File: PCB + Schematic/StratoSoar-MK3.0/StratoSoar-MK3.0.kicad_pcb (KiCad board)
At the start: 4 copper layers, 36.6 x 55.2 mm, 81 parts, among them J1 Signal, J2 Power, J3 Button, J4 USB-C, J5 J Link, J6 Antenna, J7 Battery, J8 Rudder, J9 Rudder, Q1 BSS138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

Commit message: Silkscreen!
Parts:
- removed J6: Antenna, Connector_PinHeader_2.54mm:PinHeader_1x01_P2.54mm_Vertical
- removed JP2: ERR_LED_EN, Jumper:SolderJumper-2_P1.3mm_Open_RoundedPad1.0x1.5mm
- added AE2: Antenna, Connector_PinHeader_2.54mm:PinHeader_1x01_P2.54mm_Vertical, B.Cu at (159.8, 98.8)
- added G***: LOGO, LOGO, B.Cu at (176.2, 96.2)
- added G***: LOGO, LOGO, B.Cu at (132.1, 108.1)
- JP1: value LED_EN -> ALWAYS_ON
- moved JP1 21.6 mm to (183.5, 104.5), turned to 180 degrees
- moved J4 0.73 mm to (190.8, 94.1)
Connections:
- JP1 pad 1: Net-(JP3-A) -> VCC
- JP1 pad 2: LED -> +BATT
- R10 pad 2: Net-(JP3-A) -> LED
- R14 pad 2: Net-(JP2-A) -> ERR
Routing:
- net VCC: track 55.2 -> 61.7 mm, vias 1 -> 2
- net +BATT: track 40.2 -> 43.7 mm
- net D-: track 23.8 -> 25.1 mm
- net Net-(JP3-A): track 1.13 -> 0.00 mm, vias 1 -> 0
- net Net-(JP2-A): track 1.13 -> 0.00 mm, vias 1 -> 0
- net ERR: track 9.07 -> 8.19 mm, vias 1 -> 0
- net D+: track 22.3 -> 23.1 mm
- net GND: track 102.3 -> 103.0 mm
- net Net-(J4-CC2): track 1.66 -> 2.39 mm
- net Net-(J4-CC1): track 1.70 -> 2.42 mm
- net LED: track 4.22 -> 3.66 mm, vias 1 -> 0
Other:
- board text added: "BTN"
- board text added: "Designed by Charlie Nicholson, July 2024"
- board text added: "EEPROM"
- board text added: "JLCJLCJLCJLC"
- board text added: "JP1 = Solder to enable always on"
- board text added: "Left servo-"
- board text added: "Licensed under CERN-OHL-S-2.0"
- board text added: "OFF"
- board text added: "ON"
- board text added: "RF"
- board text added: "Right servo-"
- board text added: "USB"
- board text added: "https://github.com/ crnicholson/StratoSoar-MK3"

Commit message: RF, silkscreen
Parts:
- added G***: LOGO, LOGO, B.Cu at (176.8, 83.7)
- added G***: LOGO, LOGO, B.Cu at (176.9, 88.5)
- moved G*** 11.5 mm to (169.3, 105.4)
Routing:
- net CS: track 34.1 -> 44.8 mm
- net R_FET: track 29.1 -> 39.2 mm
- net MOSI: track 44.4 -> 54.5 mm
- net MISO: track 37.1 -> 46.6 mm
- net SCK: track 39.4 -> 47.5 mm
- net RIGHT: track 39.4 -> 46.2 mm
- net LEFT: track 43.7 -> 50.1 mm
- net L_FET: track 59.7 -> 64.4 mm
- net Net-(AE2-Pin_1): track 21.6 -> 23.3 mm
- net BATT: track 32.2 -> 33.9 mm
- net SWCLK: track 11.8 -> 13.4 mm
- net SCL: track 57.9 -> 56.2 mm
- net SDA: track 60.2 -> 59.1 mm
- net GPS_EN: track 42.5 -> 43.3 mm
- net GND: track 103.0 -> 102.9 mm, vias 78 -> 84
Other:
- board text added: "Made possible by:"
- board text added: "NEWbs"
- board text added: "New England Weather Balloon Society"

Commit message: Finished PCB
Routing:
- net SCK: track 47.5 -> 57.6 mm
- net MISO: track 46.6 -> 51.2 mm, vias 2 -> 1
- net MOSI: track 54.5 -> 57.7 mm
- net L_FET: track 64.4 -> 63.4 mm
- net CS: track 44.8 -> 43.9 mm
- net R_FET: track 39.2 -> 39.9 mm
- net GND: vias 84 -> 106
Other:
- board text added: "POWER"

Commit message: Actually finished board for real?
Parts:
- added H3: MountingHole, MountingHole:MountingHole_2.2mm_M2, F.Cu at (2.48, 2.48)
- C14, C9: footprint Capacitor_SMD:C_0402_1005Metric -> Capacitor_SMD:C_0603_1608Metric
- U1: value AT24C512C-SSHD-T -> AT24C512C-SSHM-T
- U3: value AT24CS32-STUM -> BL24C32F-RRRC
- moved C9 0.43 mm to (187.0, 82.7)
- moved C14 0.33 mm to (187.9, 88.1)
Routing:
- net GND: track 102.9 -> 106.7 mm, vias 106 -> 110
- net SCL: track 56.2 -> 53.6 mm
- net Net-(AE2-Pin_1): track 23.3 -> 22.8 mm

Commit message: Actually finished board, did GPS work
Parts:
- added REF**: ESD-Logo_6.6x6mm_SilkScreen, Symbol:ESD-Logo_6.6x6mm_SilkScreen, B.Cu at (189.2, 94.0)
- added REF**: OSHW-Symbol_6.7x6mm_SilkScreen, Symbol:OSHW-Symbol_6.7x6mm_SilkScreen, B.Cu at (183.9, 74.8)

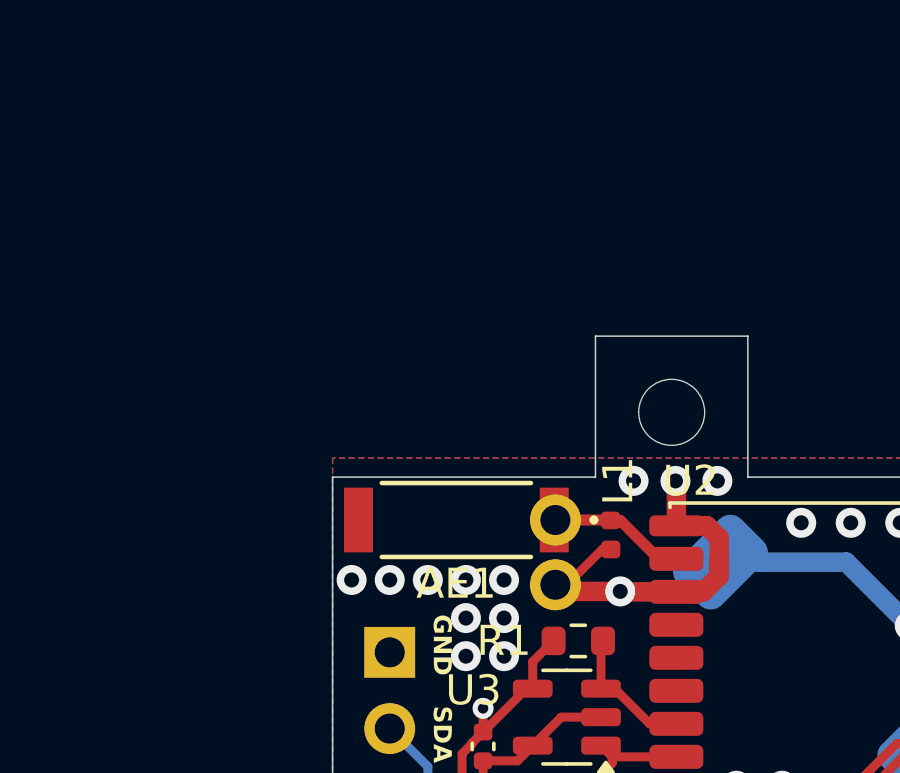
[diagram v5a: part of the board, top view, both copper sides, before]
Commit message: LoRa PCB
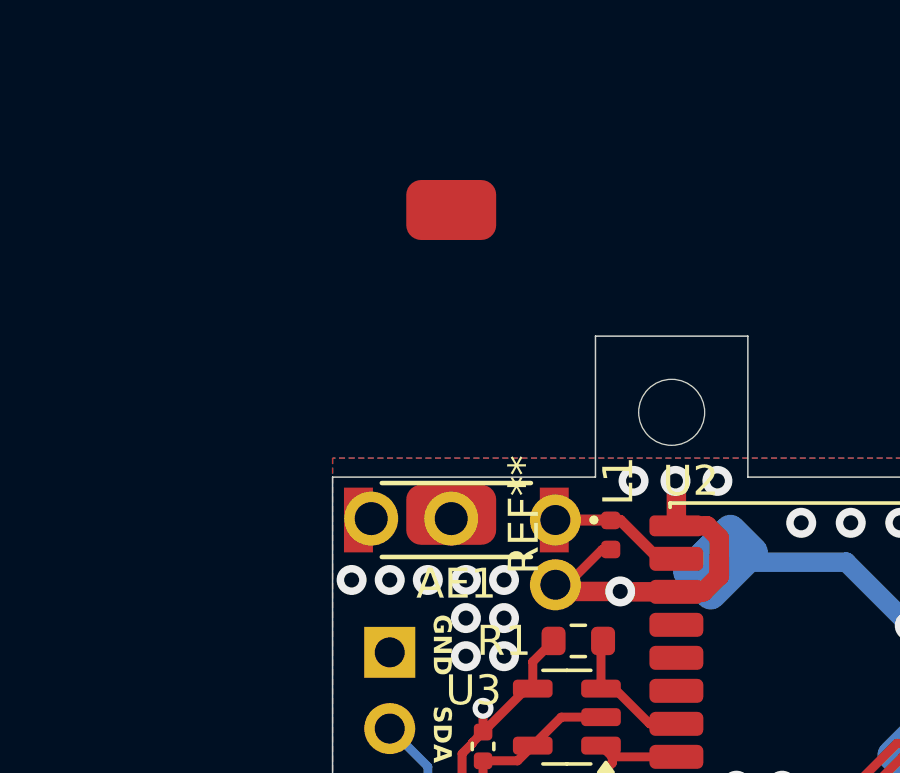
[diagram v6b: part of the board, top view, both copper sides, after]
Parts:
- added REF**: GPS1003, RF_Antenna:GPS1003, F.Cu at (161.8, 70.1)
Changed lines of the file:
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@@
+		)
+	)
+	(footprint "RF_Antenna:GPS1003"
+		(layer "F.Cu")
+		(at 161.8155 70.0905 90)
+		(property "Reference" "REF**"
+			(at 0 2.421 90)
+			(unlocked yes)
+			(layer "F.SilkS")
+			(effects
+				(font
+					(size 1 1)
+					(thickness 0.15)
+				)
+			)
+		)
+		(property "Value" "GPS1003"
+			(at 0 3.921 90)
+			(unlocked yes)
+			(layer "F.Fab")
+			(effects
+				(font
+					(size 1 1)
+					(thickness 0.15)
+				)
+			)
+		)
+		(property "Footprint" "RF_Antenna:GPS1003"
+			(at 0 2.921 90)
+			(unlocked yes)
+			(layer "F.Fab")
+			(hide yes)
+			(effects
+				(font
+					(size 1 1)
+					(thickness 0.15)
+				)
+			)
+		)
+		(property "Datasheet" ""
+			(at 0 0 90)
+			(unlocked yes)
+			(layer "F.Fab")
+			(hide yes)
+			(effects
+				(font
+					(size 1 1)
+					(thickness 0.15)
+				)
+			)
+		)
+		(property "Description" ""
+			(at 0 0 90)
+			(unlocked yes)
+			(layer "F.Fab")
+			(hide yes)
+			(effects
+				(font
+					(size 1 1)
+					(thickness 0.15)
+				)
+			)
+		)
+		(property "LCSC" "C239243"
+			(at 0 0 90)
+			(unlocked yes)
+			(layer "F.SilkS")
+			(hide yes)
+			(effects
+				(font
+					(size 1 1)
+					(thickness 0.15)
+				)
+			)
+		)
+		(attr smd)
+		(fp_text user "${REFERENCE}"
+			(at 0 5.421 90)
+			(unlocked yes)
+			(layer "F.Fab")
+			(effects
+				(font
+					(size 1 1)
+					(thickness 0.15)
+				)
+			)
+		)
+		(pad "1" thru_hole circle
+			(at -0.127 0 90)
+			(size 1.8 1.8)
+			(drill 1.1)
+			(layers "*.Cu" "*.Mask")
+			(remove_unused_layers no)
+		)
+		(pad "1" smd roundrect
+			(at 0 0 90)
+			(size 2 3)
+			(layers "F.Cu" "F.Paste" "F.Mask")
+			(roundrect_rratio 0.25)
+			(thermal_bridge_angle 45)
+		)
+		(pad "2" thru_hole circle
+			(at -0.127 -2.667 90)
+			(size 1.8 1.8)
+			(drill 1.1)
+			(layers "*.Cu" "*.Mask")
+			(remove_unused_layers no)
+		)
+		(pad "3" smd roundrect
+			(at 10.16 0 90)
+			(size 2 3)
+			(layers "F.Cu" "F.Paste" "F.Mask")
+			(roundrect_rratio 0.25)
+			(thermal_bridge_angle 45)
 		)
 	)

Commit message: Commit
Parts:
- removed REF**: GPS1003, RF_Antenna:GPS1003
- removed REF**: ESD-Logo_6.6x6mm_SilkScreen, Symbol:ESD-Logo_6.6x6mm_SilkScreen
- removed REF**: OSHW-Symbol_6.7x6mm_SilkScreen, Symbol:OSHW-Symbol_6.7x6mm_SilkScreen
- AE1: value 1575AT43A0040001E -> GPS1003; footprint 1575AT43A0040E:ANT_1575AT_JOT-L -> RF_Antenna:GPS1003
- C7: value 100 nF -> 10 nF
- moved AE1 2.08 mm to (160.0, 71.0), turned to 90 degrees
- moved L1 1.27 mm to (167.4, 72.0)
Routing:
- net GPS: track 4.59 -> 10.3 mm
- net GND: track 106.7 -> 106.4 mm, vias 110 -> 105
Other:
- board size 36.6 x 55.2 mm -> 36.6 x 60.3 mm
